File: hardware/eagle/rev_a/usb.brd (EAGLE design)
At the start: 49 x 22.5 mm, 41 parts, among them J1 MICRO_USB_B_HIROSE_ZX62-B-5PA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, P1 1932638-3_TE_AMP, P2 1932638-3_TE_AMP, P3 USB-A-FEMALETESTPOINT, U1 TPS2043B, U2 SN75240, U3 SN75240, U4 SN75240, U5 TUSB2036VF, X1 ABMM-6.000MHZ-B2-T

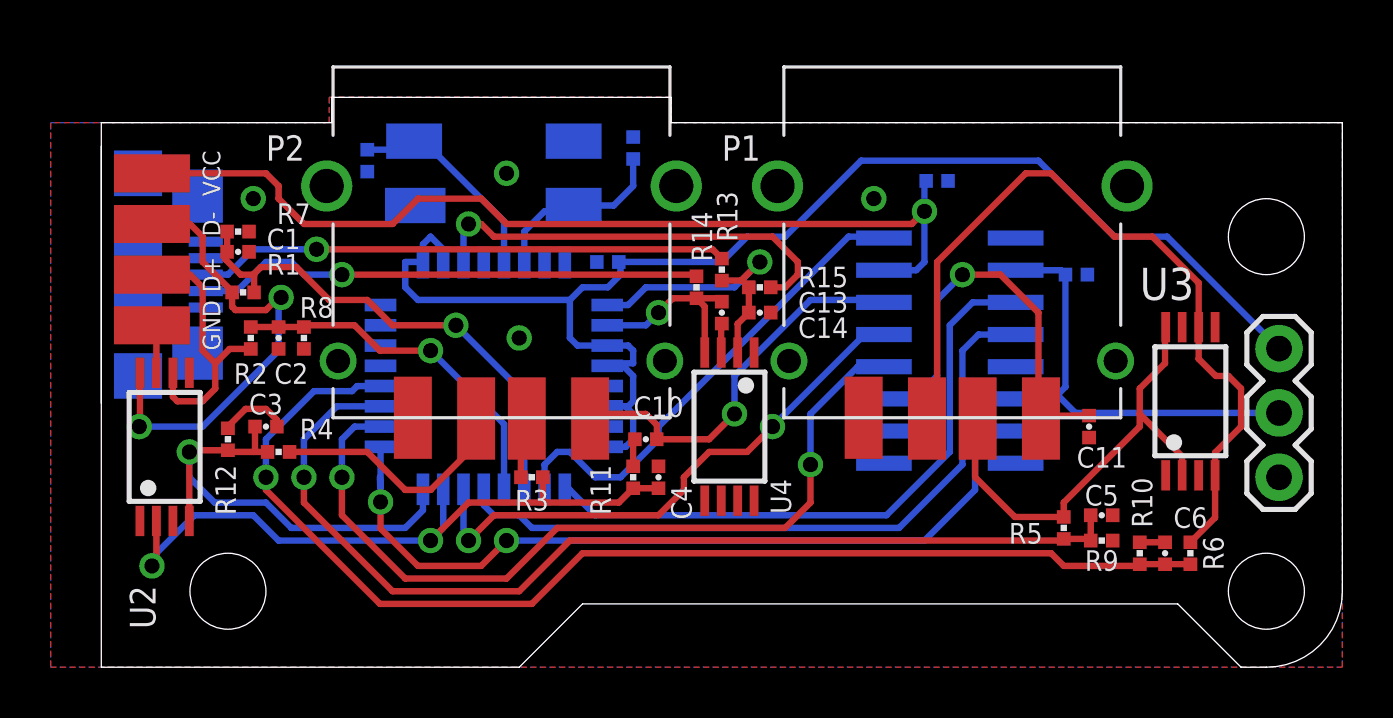
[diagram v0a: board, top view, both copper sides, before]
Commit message: Added boards for back buttons and charging/serial port Tweaks and redesigns for button/usb boards to fit in case better
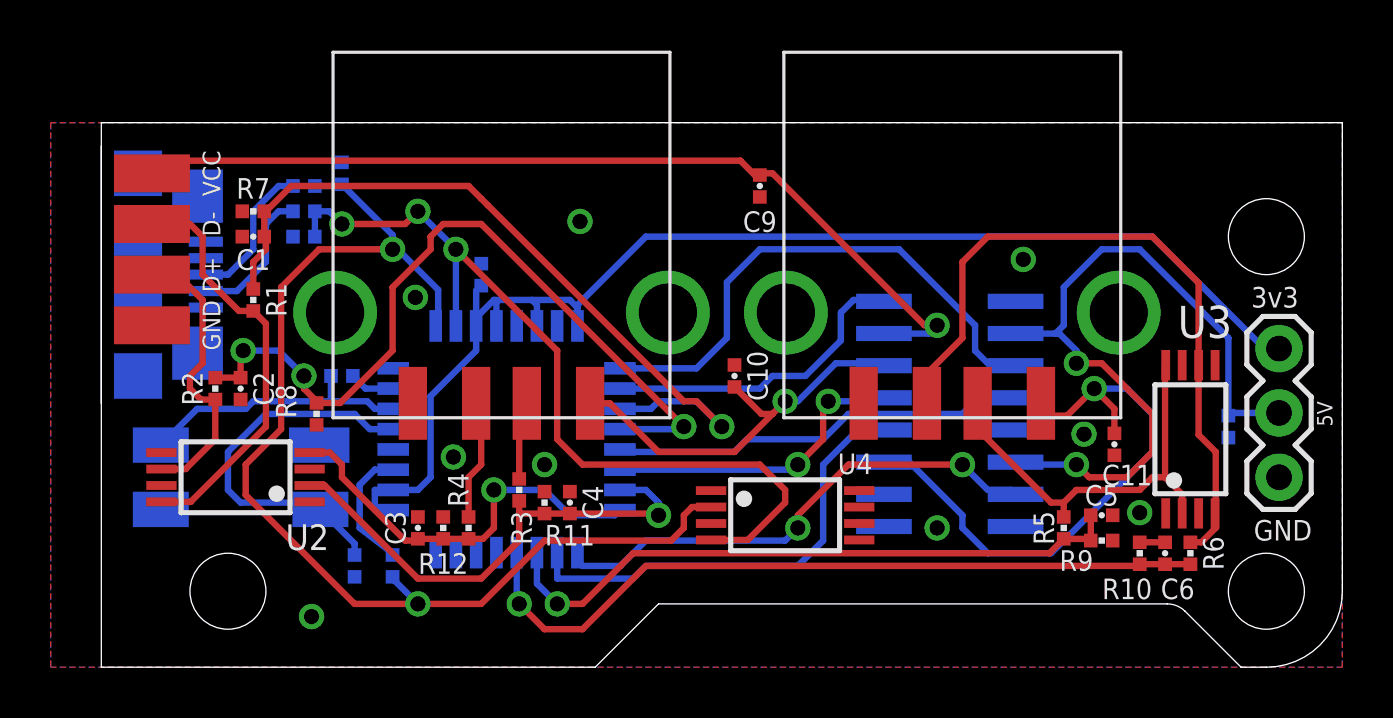
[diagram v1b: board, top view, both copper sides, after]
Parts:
- P1, P2: value 1932638-3_TE_AMP -> USB-A-FEMALE; device BMO:1932638-3_TE_AMP -> BMO:87583-3010RPALF
- moved R15 18.2 mm to (6.50, 1.00), flipped to the bottom, turned to 90 degrees
- moved C13 17.4 mm to (4.50, 16.5), flipped to the bottom, turned to 90 degrees
- moved R13 16.8 mm to (3.00, 16.0), flipped to the bottom, turned to 180 degrees
- moved C14 16.8 mm to (3.00, 14.0), flipped to the bottom, turned to 0 degrees
- moved C8 16.0 mm to (5.00, 1.00)
- moved R14 15.8 mm to (3.00, 15.0), flipped to the bottom, turned to 180 degrees
- moved X1 15.6 mm to (0.50, 4.50), turned to 180 degrees
- moved C7 14.6 mm to (4.50, 8.50), turned to 180 degrees
- moved R12 9.19 mm to (8.50, 2.50)
- moved C12 8.49 mm to (39.5, 6.50), turned to 270 degrees
- moved R4 8.08 mm to (9.50, 2.50), turned to 90 degrees
- moved C3 7.21 mm to (7.50, 2.50), turned to 90 degrees
- moved C9 7.00 mm to (21.0, 16.0), flipped to the top, turned to 270 degrees
- moved C15 5.02 mm to (10.0, 12.5), turned to 90 degrees
- moved P1 5.00 mm to (28.6, 11.0)
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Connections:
- net GND: now also P1.P$1, P1.P$2, P2.P$1, P2.P$2; no longer P1.GND0, P1.GND1, P1.GND2, P1.GND3, P2.GND0, P2.GND1, P2.GND2, P2.GND3
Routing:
- net DP0: track 11.7 -> 46.2 mm, vias 1 -> 2
- net DM0: track 7.30 -> 33.6 mm, vias 1 -> 3
- net N$18: track 14.2 -> 31.2 mm, vias 1 -> 3
- net N$22: track 46.8 -> 30.0 mm
- net N$27: track 20.9 -> 5.77 mm, vias 1 -> 0
- net N$20: track 40.5 -> 25.5 mm
- net N$21: track 32.7 -> 18.1 mm, vias 2 -> 0
- net N$26: track 20.1 -> 5.63 mm, vias 1 -> 0
- net N$15: track 33.3 -> 20.1 mm
- net VCC5V: track 17.8 -> 30.2 mm, vias 0 -> 2
- net DP0PUR: track 17.0 -> 4.98 mm, vias 1 -> 0
- net N$14: track 27.8 -> 16.6 mm
- net N$16: track 20.0 -> 30.3 mm
- net N$19: track 22.2 -> 12.4 mm
- net N$24: track 27.4 -> 19.8 mm, vias 2 -> 1
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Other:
- board size 49 x 22.5 mm -> 49 x 21.5 mm
- board text added: "3v3"
- board text added: "5V"
- board text added: "BMO USB REV A"
- board text added: "GND"
- board text added: "N.Jackson 7/16"
- board text removed: "BMO USB REV A Neal Jackson"
